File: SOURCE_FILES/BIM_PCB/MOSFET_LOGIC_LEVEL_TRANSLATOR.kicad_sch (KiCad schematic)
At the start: 0 parts

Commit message: updates on schematic and complete layout
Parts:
- added Q2: 2N7002, Package_TO_SOT_SMD:SOT-23, symbol Device:Q_NMOS_GSD
- added R16: 1K, Resistor_SMD:R_0402_1005Metric, symbol Device:R_US
- added R16, R17: 10K, Resistor_SMD:R_0402_1005Metric, symbol Device:R_US
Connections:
- new net: Q2.2 (S), R16.2, R16.2
- new net HIGH_SIDE_LOGIC_SIGNAL: Q2.3 (D), R17.2
- new net HIGH_SIDE_POWER_LEVEL: R17.1
- new net LOW_SIDE_LOGIC_SIGNAL: R16.1
- new net LOW_SIDE_POWER_LEVEL: Q2.1 (G), R16.1
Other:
- note added: "BI-DIRECTIONAL LEVEL TRANSLATOR MOSFET - IMPLEMENTATION"
- note added: "HIGH LEVEL SIDE"
- note added: "LOW LEVEL SIDE"

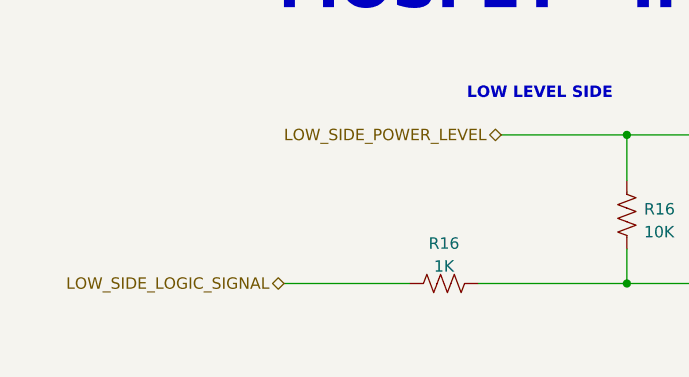
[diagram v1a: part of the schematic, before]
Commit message: completed design PCN and Images
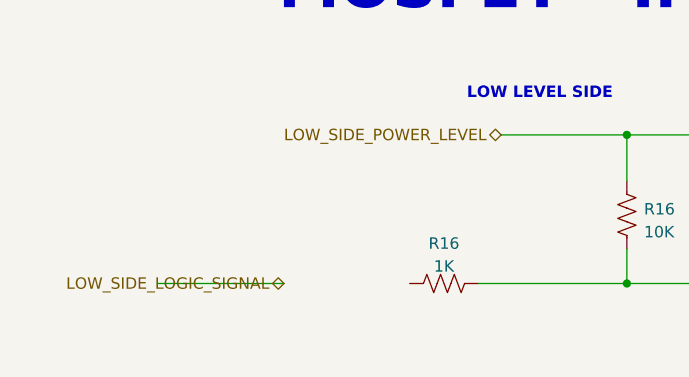
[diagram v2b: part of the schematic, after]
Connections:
- net LOW_SIDE_LOGIC_SIGNAL: no longer R16.1
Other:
- company: (none) -> GEVITON
- title: (none) -> BIM BOARD
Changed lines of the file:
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@@
 (kicad_sch (version 20230121) (generator eeschema)
   (paper "A4")
+  (title_block
+    (title "BIM BOARD")
+    (date "2023-12-06")
+    (rev "REV 2.0.0")
+    (company "GEVITON")
+    (comment 2 "Reviewed by: Timothy Kyalo")
+    (comment 3 "Designed By: Robert Mutura")
+    (comment 4 "BIM BOARD")
+  )
   (junction (at 136.525 73.66) (diameter 0) (color 0 0 0 0)
   )
@@
     (stroke (width 0) (type default))
   )
-  (wire (pts (xy 98.425 90.17) (xy 112.395 90.17))
+  (wire (pts (xy 98.425 90.17) (xy 84.455 90.17))
     (stroke (width 0) (type default))
   )

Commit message: complete BIM Board
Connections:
- net LOW_SIDE_LOGIC_SIGNAL: now also R16.1
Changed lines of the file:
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@@
     (stroke (width 0) (type default))
   )
-  (wire (pts (xy 98.425 90.17) (xy 84.455 90.17))
+  (wire (pts (xy 112.395 90.17) (xy 98.425 90.17))
     (stroke (width 0) (type default))
   )
